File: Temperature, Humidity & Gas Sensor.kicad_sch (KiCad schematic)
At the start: 5 parts, among them U7 BME690

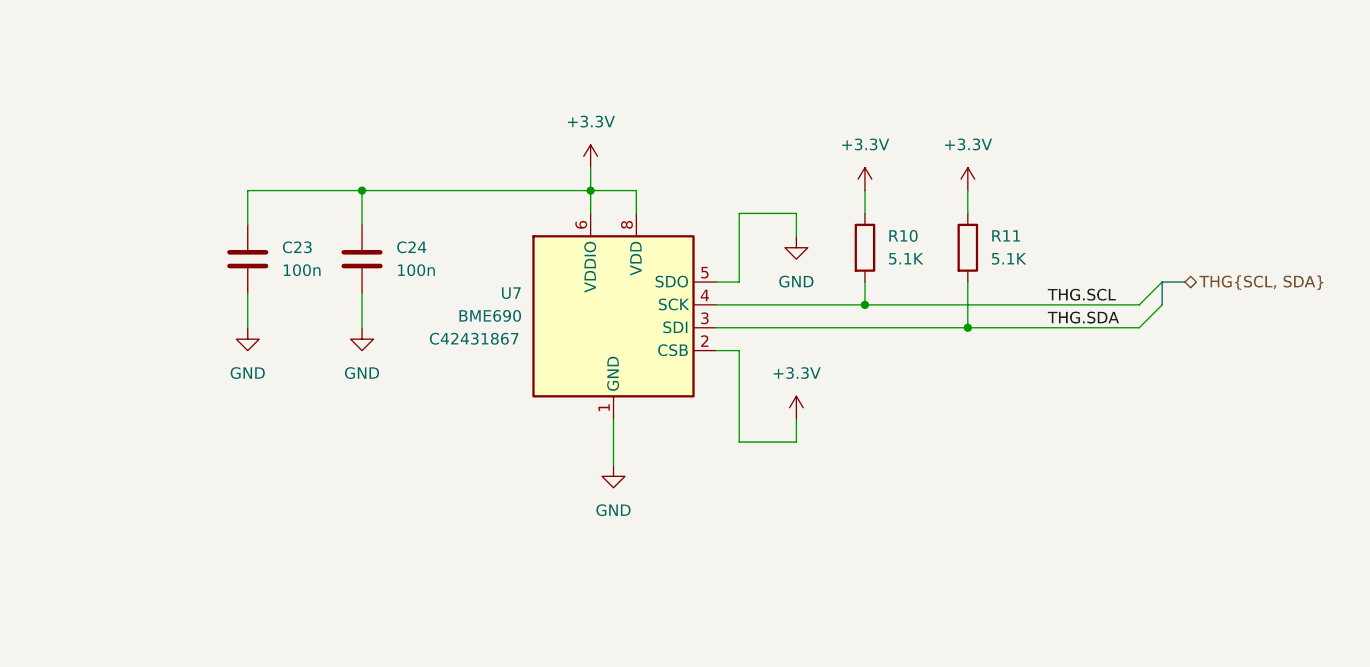
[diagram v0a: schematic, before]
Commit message: Verification
- changed the piezo electric speaker.
- verified some schematics
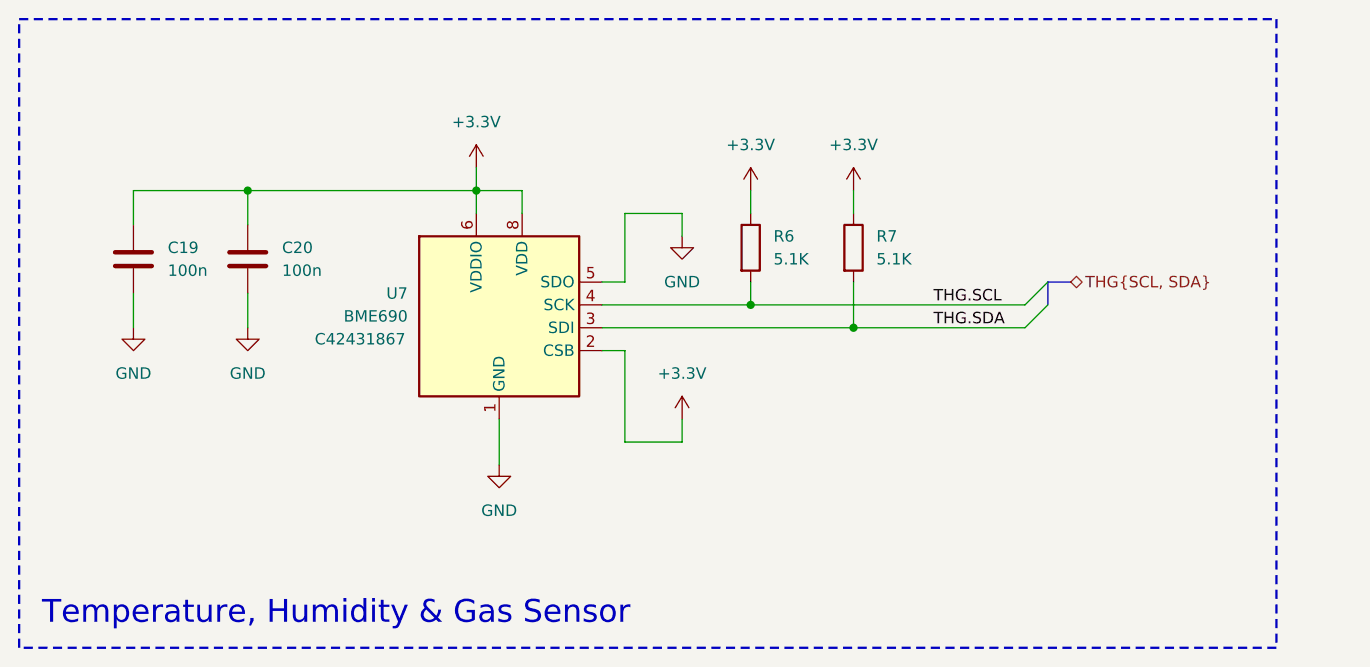
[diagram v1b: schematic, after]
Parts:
- renumbered C23 to C19, C24 to C20, R10 to R6, R11 to R7
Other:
- note added: "Temperature, Humidity & Gas Sensor"
- moved on the sheet: C19, C20, R6, R7, U7

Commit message: Verification
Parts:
- renumbered C19 to C22, C20 to C23, R6 to R11, R7 to R12
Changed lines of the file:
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@@
 	(title_block
 		(title "Temperature, Humidity & Gas Sensor")
-		(date "2026-01-29")
+		(date "2026-02-04")
 		(rev "v0.0")
 		(company "TJ71PL")
@@
 		(dnp no)
 		(fields_autoplaced yes)
-		(property "Reference" "#PWR047"
+		(property "Reference" "#PWR059"
 			(at 101.6 104.14 0)
 			(effects
@@
 			(project ""
 				(path "/c9a8ff63-a0d1-4125-9dd1-40fb53daf536/cc882cab-fb20-4552-b867-43569dfc2d06"
-					(reference "#PWR047")
+					(reference "#PWR059")
 					(unit 1)
 				)
@@
 		(dnp no)
 		(fields_autoplaced yes)
-		(property "Reference" "C19"
+		(property "Reference" "C22"
 			(at 92.71 88.8999 0)
 			(effects
@@
 			(project "Precision Clock"
 				(path "/c9a8ff63-a0d1-4125-9dd1-40fb53daf536/cc882cab-fb20-4552-b867-43569dfc2d06"
-					(reference "C19")
+					(reference "C22")
 					(unit 1)
 				)
@@
 		(dnp no)
 		(fields_autoplaced yes)
-		(property "Reference" "#PWR052"
+		(property "Reference" "#PWR064"
 			(at 157.48 86.36 0)
 			(effects
@@
 			(project "Precision Clock"
 				(path "/c9a8ff63-a0d1-4125-9dd1-40fb53daf536/cc882cab-fb20-4552-b867-43569dfc2d06"
-					(reference "#PWR052")
+					(reference "#PWR064")
 					(unit 1)
 				)
@@
 		(dnp no)
 		(fields_autoplaced yes)
-		(property "Reference" "R7"
+		(property "Reference" "R12"
 			(at 171.45 87.6299 0)
 			(effects
@@
 			(project "Precision Clock"
 				(path "/c9a8ff63-a0d1-4125-9dd1-40fb53daf536/cc882cab-fb20-4552-b867-43569dfc2d06"
-					(reference "R7")
+					(reference "R12")
 					(unit 1)
 				)
@@
 		(dnp no)
 		(fields_autoplaced yes)
-		(property "Reference" "#PWR050"
+		(property "Reference" "#PWR062"
 			(at 149.86 93.98 0)
 			(effects
@@
 			(project ""
 				(path "/c9a8ff63-a0d1-4125-9dd1-40fb53daf536/cc882cab-fb20-4552-b867-43569dfc2d06"
-					(reference "#PWR050")
+					(reference "#PWR062")
 					(unit 1)
 				)
@@
 		(dnp no)
 		(fields_autoplaced yes)
-		(property "Reference" "#PWR051"
+		(property "Reference" "#PWR063"
 			(at 149.86 111.76 0)
 			(effects
@@
 			(project "Precision Clock"
 				(path "/c9a8ff63-a0d1-4125-9dd1-40fb53daf536/cc882cab-fb20-4552-b867-43569dfc2d06"
-					(reference "#PWR051")
+					(reference "#PWR063")
 					(unit 1)
 				)
@@
 		(dnp no)
 		(fields_autoplaced yes)
-		(property "Reference" "C20"
+		(property "Reference" "C23"
 			(at 105.41 88.8999 0)
 			(effects
@@
 			(project ""
 				(path "/c9a8ff63-a0d1-4125-9dd1-40fb53daf536/cc882cab-fb20-4552-b867-43569dfc2d06"
-					(reference "C20")
+					(reference "C23")
 					(unit 1)
 				)
@@
 		(dnp no)
 		(fields_autoplaced yes)
-		(property "Reference" "#PWR046"
+		(property "Reference" "#PWR058"
 			(at 88.9 104.14 0)
 			(effects
@@
 			(project "Precision Clock"
 				(path "/c9a8ff63-a0d1-4125-9dd1-40fb53daf536/cc882cab-fb20-4552-b867-43569dfc2d06"
-					(reference "#PWR046")
+					(reference "#PWR058")
 					(unit 1)
 				)
@@
 		(dnp no)
 		(fields_autoplaced yes)
-		(property "Reference" "R6"
+		(property "Reference" "R11"
 			(at 160.02 87.6299 0)
 			(effects
@@
 			(project ""
 				(path "/c9a8ff63-a0d1-4125-9dd1-40fb53daf536/cc882cab-fb20-4552-b867-43569dfc2d06"
-					(reference "R6")
+					(reference "R11")
 					(unit 1)
 				)
@@
 		(dnp no)
 		(fields_autoplaced yes)
-		(property "Reference" "#PWR049"
+		(property "Reference" "#PWR061"
 			(at 129.54 119.38 0)
 			(effects
@@
 			(project ""
 				(path "/c9a8ff63-a0d1-4125-9dd1-40fb53daf536/cc882cab-fb20-4552-b867-43569dfc2d06"
-					(reference "#PWR049")
+					(reference "#PWR061")
 					(unit 1)
 				)
@@
 		(dnp no)
 		(fields_autoplaced yes)
-		(property "Reference" "#PWR048"
+		(property "Reference" "#PWR060"
 			(at 127 83.82 0)
 			(effects
@@
 			(project ""
 				(path "/c9a8ff63-a0d1-4125-9dd1-40fb53daf536/cc882cab-fb20-4552-b867-43569dfc2d06"
-					(reference "#PWR048")
+					(reference "#PWR060")
 					(unit 1)
 				)
@@
 		(dnp no)
 		(fields_autoplaced yes)
-		(property "Reference" "#PWR053"
+		(property "Reference" "#PWR065"
 			(at 168.91 86.36 0)
 			(effects
@@
 			(project "Precision Clock"
 				(path "/c9a8ff63-a0d1-4125-9dd1-40fb53daf536/cc882cab-fb20-4552-b867-43569dfc2d06"
-					(reference "#PWR053")
+					(reference "#PWR065")
 					(unit 1)
 				)

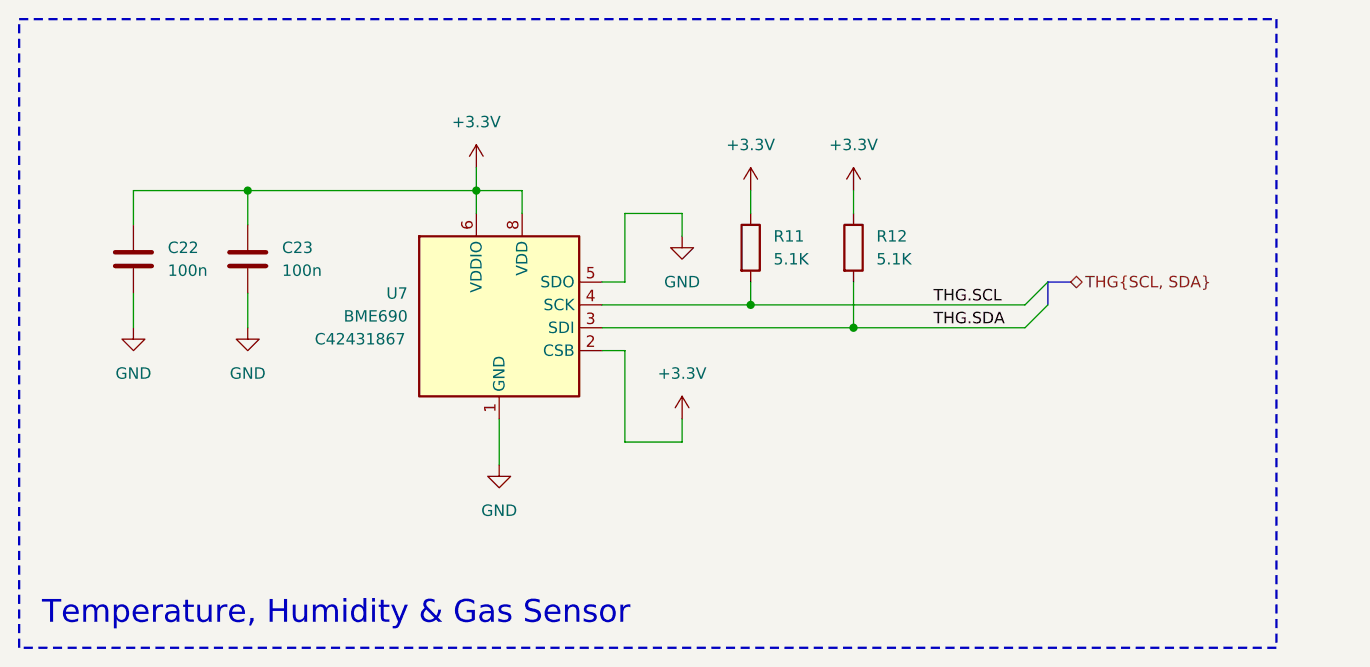
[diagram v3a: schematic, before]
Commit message: display driver update
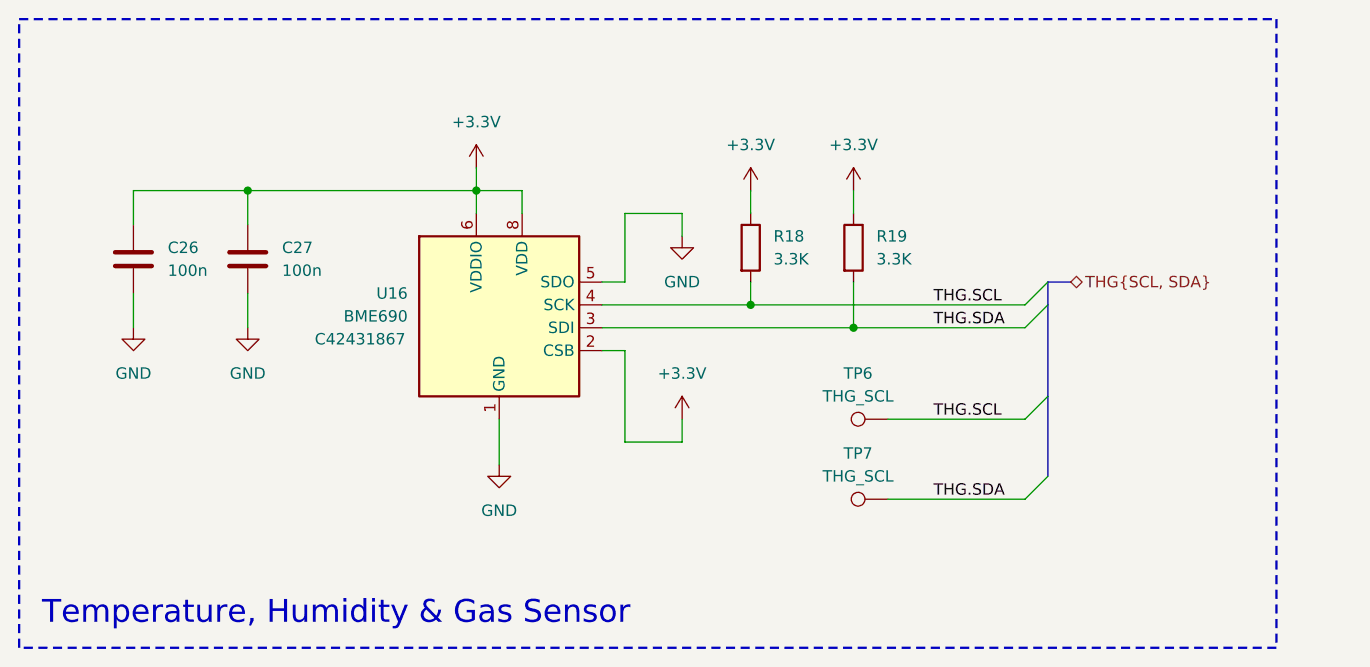
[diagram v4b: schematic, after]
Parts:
- added TP6, TP7: THG_SCL, TestPoint:TestPoint_Pad_D1.0mm, symbol Connector:TestPoint
- R18: renamed from R11; value 5.1K -> 3.3K
- R19: renamed from R12; value 5.1K -> 3.3K
- renumbered C22 to C26, C23 to C27, U7 to U16
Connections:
- net THG.SCL: now also TP6.1
- net THG.SDA: now also TP7.1

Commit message: Display Driver Completion
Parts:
- removed U16: BME690, Package_LGA:Bosch_LGA-8_3x3mm_P0.8mm_ClockwisePinNumbering, symbol precision_clock:BME690
- added U14: BME690, Package_LGA:Bosch_LGA-8_3x3mm_P0.8mm_ClockwisePinNumbering, symbol precision_clock:BME690
- R7: renamed from R18; value 3.3K -> 10K
- R8: renamed from R19; value 3.3K -> 10K
- renumbered C26 to C29, C27 to C30, TP6 to TP17, TP7 to TP18
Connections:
- net +3.3V: now also U14.2 (CSB), U14.6 (VDDIO), U14.8 (VDD)
- net GND: now also U14.1 (GND), U14.5 (SDO), U14.7 (GND)
- net THG.SCL: now also U14.4 (SCK)
- net THG.SDA: now also U14.3 (SDI)
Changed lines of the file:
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@@
 	(title_block
 		(title "Temperature, Humidity & Gas Sensor")
-		(date "2026-02-04")
+		(date "2026-02-06")
 		(rev "v0.0")
 		(company "TJ71PL")
 		(comment 1 "天計")
 		(comment 4 "Final verification complete")
+	)
+	(bus_alias "THG_BUS"
+		(members "THG.SCL" "THG.SDA")
 	)
 	(rectangle
@@
 		)
 	)
-	(hierarchical_label "THG{SCL, SDA}"
+	(hierarchical_label "{THG_BUS}"
 		(shape bidirectional)
 		(at 193.04 92.71 0)
@@
 		(dnp no)
 		(fields_autoplaced yes)
-		(property "Reference" "#PWR067"
+		(property "Reference" "#PWR074"
 			(at 101.6 104.14 0)
 			(effects
@@
 			(project ""
 				(path "/c9a8ff63-a0d1-4125-9dd1-40fb53daf536/cc882cab-fb20-4552-b867-43569dfc2d06"
-					(reference "#PWR067")
+					(reference "#PWR074")
 					(unit 1)
 				)
@@
 		(dnp no)
 		(fields_autoplaced yes)
-		(property "Reference" "C26"
+		(property "Reference" "C29"
 			(at 92.71 88.8999 0)
 			(effects
@@
 			(project "Precision Clock"
 				(path "/c9a8ff63-a0d1-4125-9dd1-40fb53daf536/cc882cab-fb20-4552-b867-43569dfc2d06"
-					(reference "C26")
+					(reference "C29")
 					(unit 1)
 				)
@@
 		(dnp no)
 		(fields_autoplaced yes)
-		(property "Reference" "TP6"
+		(property "Reference" "TP17"
 			(at 169.418 102.87 90)
 			(effects
@@
 			(project ""
 				(path "/c9a8ff63-a0d1-4125-9dd1-40fb53daf536/cc882cab-fb20-4552-b867-43569dfc2d06"
-					(reference "TP6")
+					(reference "TP17")
 					(unit 1)
 				)
@@
 		(dnp no)
 		(fields_autoplaced yes)
-		(property "Reference" "#PWR072"
+		(property "Reference" "#PWR079"
 			(at 157.48 86.36 0)
 			(effects
@@
 			(project "Precision Clock"
 				(path "/c9a8ff63-a0d1-4125-9dd1-40fb53daf536/cc882cab-fb20-4552-b867-43569dfc2d06"
-					(reference "#PWR072")
+					(reference "#PWR079")
 					(unit 1)
 				)
@@
 		(dnp no)
 		(fields_autoplaced yes)
-		(property "Reference" "R19"
+		(property "Reference" "R8"
 			(at 171.45 87.6299 0)
 			(effects
@@
 			)
 		)
-		(property "Value" "3.3K"
+		(property "Value" "10K"
 			(at 171.45 90.1699 0)
 			(effects
@@
 			(project "Precision Clock"
 				(path "/c9a8ff63-a0d1-4125-9dd1-40fb53daf536/cc882cab-fb20-4552-b867-43569dfc2d06"
-					(reference "R19")
+					(reference "R8")
 					(unit 1)
 				)
@@
 		(dnp no)
 		(fields_autoplaced yes)
-		(property "Reference" "#PWR070"
+		(property "Reference" "#PWR077"
 			(at 149.86 93.98 0)
 			(effects
@@
 			(project ""
 				(path "/c9a8ff63-a0d1-4125-9dd1-40fb53daf536/cc882cab-fb20-4552-b867-43569dfc2d06"
-					(reference "#PWR070")
+					(reference "#PWR077")
 					(unit 1)
 				)
@@
 		(dnp no)
 		(fields_autoplaced yes)
-		(property "Reference" "#PWR071"
+		(property "Reference" "#PWR078"
 			(at 149.86 111.76 0)
 			(effects
@@
 			(project "Precision Clock"
 				(path "/c9a8ff63-a0d1-4125-9dd1-40fb53daf536/cc882cab-fb20-4552-b867-43569dfc2d06"
-					(reference "#PWR071")
+					(reference "#PWR078")
 					(unit 1)
 				)
@@
 		(dnp no)
 		(fields_autoplaced yes)
-		(property "Reference" "C27"
+		(property "Reference" "C30"
 			(at 105.41 88.8999 0)
 			(effects
@@
 			(project ""
 				(path "/c9a8ff63-a0d1-4125-9dd1-40fb53daf536/cc882cab-fb20-4552-b867-43569dfc2d06"
-					(reference "C27")
-					(unit 1)
-				)
-			)
-		)
-	)
-	(symbol
-		(lib_id "precision_clock:BME690")
-		(at 129.54 96.52 0)
-		(unit 1)
-		(exclude_from_sim no)
-		(in_bom yes)
-		(on_board yes)
-		(dnp no)
-		(property "Reference" "U16"
-			(at 119.38 93.98 0)
-			(effects
-				(font
-					(size 1.27 1.27)
-				)
-				(justify right)
-			)
-		)
-		(property "Value" "BME690"
-			(at 119.38 96.52 0)
-			(effects
-				(font
-					(size 1.27 1.27)
-				)
-				(justify right)
-			)
-		)
-		(property "Footprint" "Package_LGA:Bosch_LGA-8_3x3mm_P0.8mm_ClockwisePinNumbering"
-			(at 129.54 96.52 0)
-			(effects
-				(font
-					(size 1.27 1.27)
-				)
-				(hide yes)
-			)
-		)
-		(property "Datasheet" "https://www.bosch-sensortec.com/products/environmental-sensors/gas-sensors/bme690/"
-			(at 129.54 96.52 0)
-			(effects
-				(font
-					(size 1.27 1.27)
-				)
-				(hide yes)
-			)
-		)
-		(property "Description" "4-in-1 sensor, gas, humidity, pressure, temperature, I2C and SPI interface, 1.71-3.6V, LGA-8"
-			(at 129.54 96.52 0)
-			(effects
-				(font
-					(size 1.27 1.27)
-				)
-				(hide yes)
-			)
-		)
-		(property "LCSC" "C42431867"
-			(at 119.126 99.0601 0)
-			(effects
-				(font
-					(size 1.27 1.27)
-				)
-				(justify right)
-			)
-		)
-		(pin "1"
-		)
-		(pin "6"
-		)
-		(pin "8"
-		)
-		(pin "5"
-		)
-		(pin "7"
-		)
-		(pin "3"
-		)
-		(pin "4"
-		)
-		(pin "2"
-		)
-		(instances
-			(project ""
-				(path "/c9a8ff63-a0d1-4125-9dd1-40fb53daf536/cc882cab-fb20-4552-b867-43569dfc2d06"
-					(reference "U16")
+					(reference "C30")
 					(unit 1)
 				)
@@
 		(dnp no)
 		(fields_autoplaced yes)
-		(property "Reference" "#PWR066"
+		(property "Reference" "#PWR073"
 			(at 88.9 104.14 0)
 			(effects
@@
 			(project "Precision Clock"
 				(path "/c9a8ff63-a0d1-4125-9dd1-40fb53daf536/cc882cab-fb20-4552-b867-43569dfc2d06"
-					(reference "#PWR066")
+					(reference "#PWR073")
 					(unit 1)
 				)
@@
 		(dnp no)
 		(fields_autoplaced yes)
-		(property "Reference" "R18"
+		(property "Reference" "R7"
 			(at 160.02 87.6299 0)
 			(effects
@@
 			)
 		)
-		(property "Value" "3.3K"
+		(property "Value" "10K"
 			(at 160.02 90.1699 0)
 			(effects
@@
 			(project ""
 				(path "/c9a8ff63-a0d1-4125-9dd1-40fb53daf536/cc882cab-fb20-4552-b867-43569dfc2d06"
-					(reference "R18")
+					(reference "R7")
 					(unit 1)
 				)
@@
 		(dnp no)
 		(fields_autoplaced yes)
-		(property "Reference" "#PWR069"
+		(property "Reference" "#PWR076"
 			(at 129.54 119.38 0)
 			(effects
@@
 			(project ""
 				(path "/c9a8ff63-a0d1-4125-9dd1-40fb53daf536/cc882cab-fb20-4552-b867-43569dfc2d06"
-					(reference "#PWR069")
+					(reference "#PWR076")
 					(unit 1)
 				)
@@
 		(dnp no)
 		(fields_autoplaced yes)
-		(property "Reference" "#PWR068"
+		(property "Reference" "#PWR075"
 			(at 127 83.82 0)
 			(effects
@@
 			(project ""
 				(path "/c9a8ff63-a0d1-4125-9dd1-40fb53daf536/cc882cab-fb20-4552-b867-43569dfc2d06"
-					(reference "#PWR068")
+					(reference "#PWR075")
 					(unit 1)
 				)
@@
 		(dnp no)
 		(fields_autoplaced yes)
-		(property "Reference" "#PWR073"
+		(property "Reference" "#PWR080"
 			(at 168.91 86.36 0)
 			(effects
@@
 			(project "Precision Clock"
 				(path "/c9a8ff63-a0d1-4125-9dd1-40fb53daf536/cc882cab-fb20-4552-b867-43569dfc2d06"
-					(reference "#PWR073")
+					(reference "#PWR080")
+					(unit 1)
+				)
+			)
+		)
+	)
+	(symbol
+		(lib_id "precision_clock:BME690")
+		(at 129.54 96.52 0)
+		(unit 1)
+		(exclude_from_sim no)
+		(in_bom yes)
+		(on_board yes)
+		(dnp no)
+		(fields_autoplaced yes)
+		(property "Reference" "U14"
+			(at 119.38 95.2499 0)
+			(effects
+				(font
+					(size 1.27 1.27)
+				)
+				(justify right)
+			)
+		)
+		(property "Value" "BME690"
+			(at 119.38 97.7899 0)
+			(effects
+				(font
+					(size 1.27 1.27)
+				)
+				(justify right)
+			)
+		)
+		(property "Footprint" "Package_LGA:Bosch_LGA-8_3x3mm_P0.8mm_ClockwisePinNumbering"
+			(at 129.54 96.52 0)
+			(effects
+				(font
+					(size 1.27 1.27)
+				)
+				(hide yes)
+			)
+		)
+		(property "Datasheet" "https://www.bosch-sensortec.com/products/environmental-sensors/gas-sensors/bme690/"
+			(at 129.54 96.52 0)
+			(effects
+				(font
+					(size 1.27 1.27)
+				)
+				(hide yes)
+			)
+		)
+		(property "Description" "4-in-1 sensor, gas, humidity, pressure, temperature, I2C and SPI interface, 1.71-3.6V, LGA-8"
+			(at 129.54 96.52 0)
+			(effects
+				(font
+					(size 1.27 1.27)
+				)
+				(hide yes)
+			)
+		)
+		(pin "5"
+		)
+		(pin "4"
+		)
+		(pin "2"
+		)
+		(pin "3"
+		)
+		(pin "6"
+		)
+		(pin "1"
+		)
+		(pin "7"
+		)
+		(pin "8"
+		)
+		(instances
+			(project ""
+				(path "/c9a8ff63-a0d1-4125-9dd1-40fb53daf536/cc882cab-fb20-4552-b867-43569dfc2d06"
+					(reference "U14")
 					(unit 1)
 				)
@@
 		(dnp no)
 		(fields_autoplaced yes)
-		(property "Reference" "TP7"
+		(property "Reference" "TP18"
 			(at 169.418 111.76 90)
 			(effects
@@
 			(project "Precision Clock"
 				(path "/c9a8ff63-a0d1-4125-9dd1-40fb53daf536/cc882cab-fb20-4552-b867-43569dfc2d06"
-					(reference "TP7")
+					(reference "TP18")
 					(unit 1)
 				)
